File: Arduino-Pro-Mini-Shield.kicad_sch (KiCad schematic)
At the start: 9 parts, among them CON1 AVR-ISP-6, IC1 ArduinoProMini, J1 Conn_01x03, J2 Conn_02x09_Odd_Even, J3 Conn_01x03, J4 Conn_02x04_Odd_Even

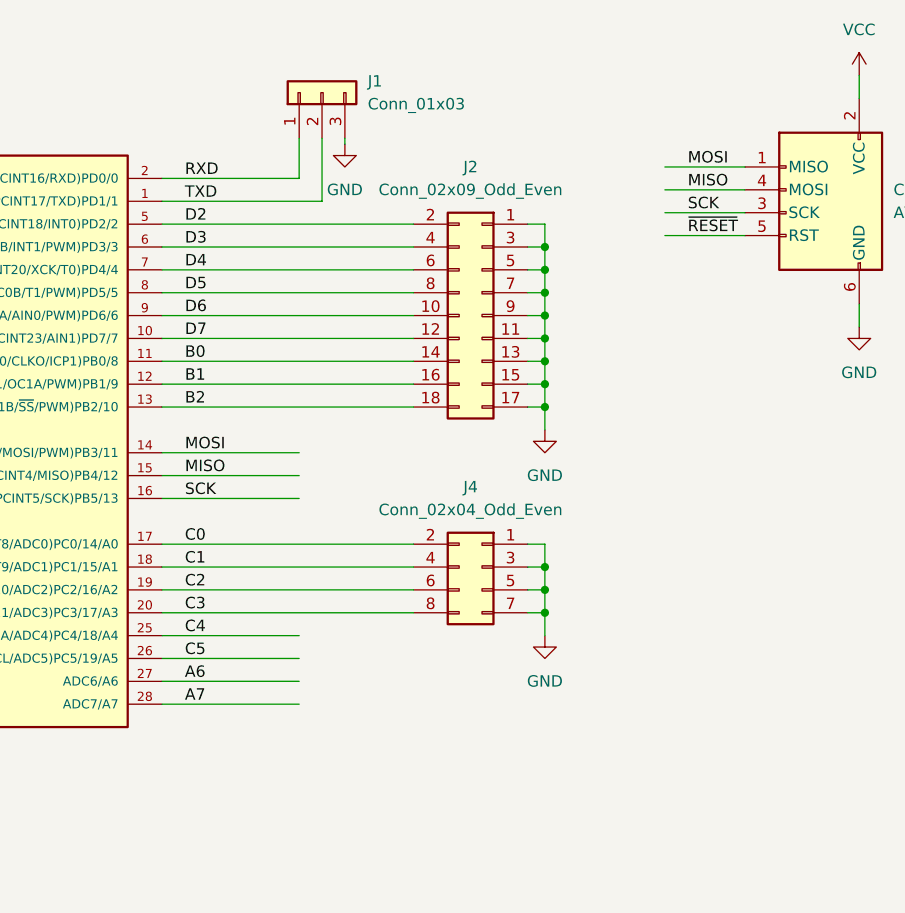
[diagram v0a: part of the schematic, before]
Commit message: BUGFIX: swapped MOSI and MISO
added also pins for SPI and I2C
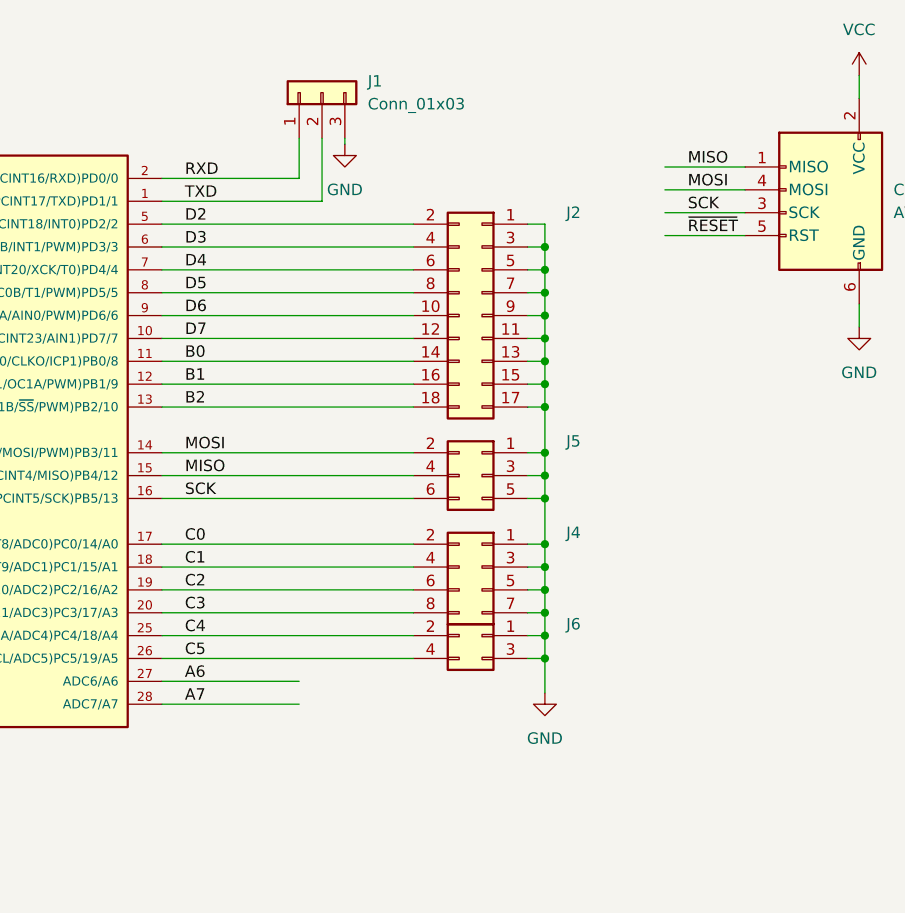
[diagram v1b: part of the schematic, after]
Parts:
- added J5: Conn_02x03_Odd_Even, Connector_PinHeader_2.54mm:PinHeader_2x03_P2.54mm_Vertical, symbol Connector_Generic:Conn_02x03_Odd_Even
- added J6: Conn_02x02_Odd_Even, Connector_PinHeader_2.54mm:PinHeader_2x02_P2.54mm_Vertical, symbol Connector_Generic:Conn_02x02_Odd_Even
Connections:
- net C4: now also J6.2 (Pin_2)
- net C5: now also J6.4 (Pin_4)
- net GND: now also J5.1 (Pin_1), J5.3 (Pin_3), J5.5 (Pin_5), J6.1 (Pin_1), J6.3 (Pin_3)
- net MISO: now also CON1.1 (MISO), J5.4 (Pin_4); no longer CON1.4 (MOSI)
- net MOSI: now also CON1.4 (MOSI), J5.2 (Pin_2); no longer CON1.1 (MISO)
- net SCK: now also J5.6 (Pin_6)
